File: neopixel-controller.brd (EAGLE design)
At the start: 23.8 x 26.7 mm, 10 parts, among them J1 Power, U1 ATTiny85

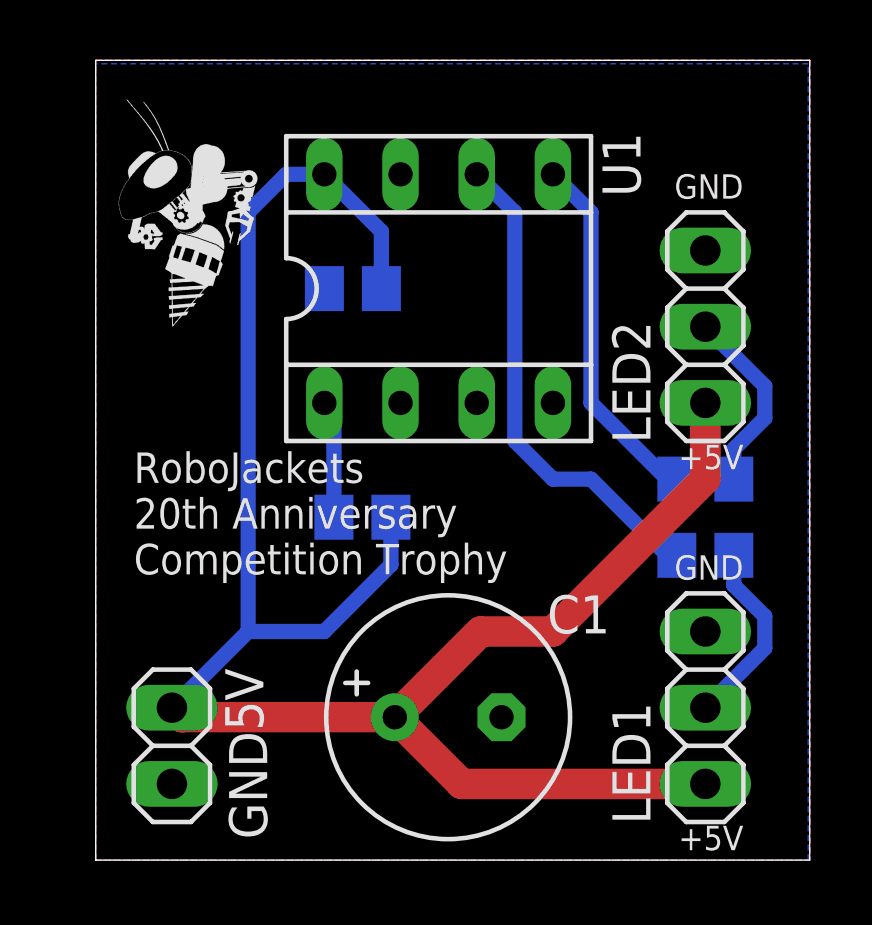
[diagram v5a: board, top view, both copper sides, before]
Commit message: Reroute original controller to use a SOIC ATtiny85
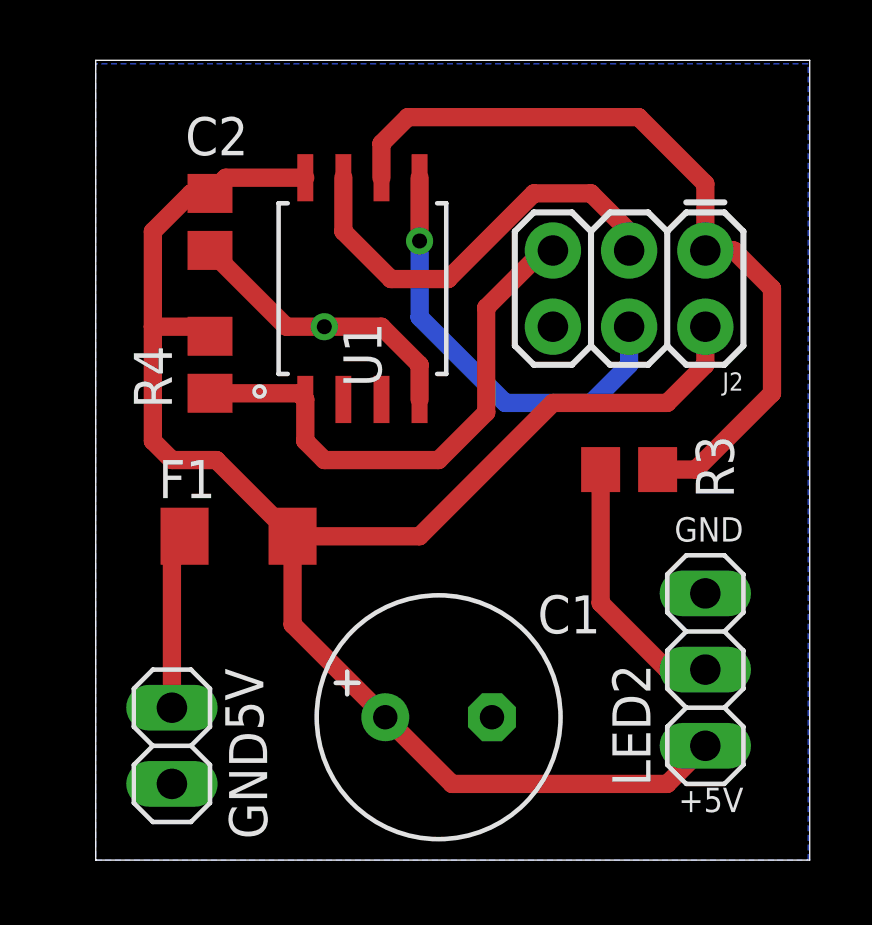
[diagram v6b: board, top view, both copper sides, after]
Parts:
- removed LED1: Neopixel, JoshCustom:NEOPIXEL_PINHEAD
- removed R2: 470, resistor:R0805
- added F1: 250mA, JoshCustom:F1206
- added J2: AVR_SPI_PROG_3X2PTH, SparkFun-Connectors:2X3
- U1: value ATTiny85 -> ATTINY85; device JoshCustom:SOCKET-08 -> JoshCustom:8S2
- moved LED2 11.4 mm to (20.3, 6.35)
- moved R4 7.18 mm to (3.81, 16.5), flipped to the top, turned to 90 degrees
- moved C2 5.26 mm to (3.81, 21.3), flipped to the top, turned to 270 degrees
- moved R3 2.56 mm to (17.8, 13.0), flipped to the top
- moved U$1 2.54 mm to (5.08, 17.8), flipped to the bottom
- moved U1 2.54 mm to (8.89, 19.1), turned to 90 degrees
- moved C1 0.32 mm to (11.4, 4.76)
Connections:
- removed net LED1: R2.1, U1.6
- removed net LED2: R3.1, U1.5
- removed net N$5: R4.1, U1.1
- new net !RESET!: J2.5, R4.1, U1.1
- new net MISO: J2.1, R3.1, U1.6
- new net MOSI: J2.4, U1.5
- new net SCK: J2.3, U1.7
- net GND: now also J2.6; no longer LED1.3
- net N$2: now also F1.1, J1.1; no longer LED1.2, R2.2
- net VCC: now also F1.2, J2.2; no longer J1.1, LED1.1
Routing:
- net MISO: track 0.00 -> 26.5 mm
- net !RESET!: track 0.00 -> 18.1 mm
- net LED1: track 16.7 -> 0.00 mm
- net MOSI: track 0.00 -> 14.6 mm, vias 0 -> 1
- net SCK: track 0.00 -> 14.3 mm
- net LED2: track 12.1 -> 0.00 mm
- net VCC: track 67.5 -> 57.6 mm
- net GND: track 0.00 -> 9.72 mm, vias 0 -> 1
- net N$5: track 3.94 -> 0.00 mm
- net N$1: track 6.33 -> 8.86 mm
- removed copper zone on layer 1, net GND
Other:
- board text added: "v1.2, March 2019"
- board text removed: "ATtiny85"
- board text removed: "v1.1, Feb. 2019"
